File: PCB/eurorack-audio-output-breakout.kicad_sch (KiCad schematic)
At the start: 23 parts, among them J1 upper, J2 lower, J3 Conn_01x04_Pin, J4 Conn_01x02_Pin, J6 Conn_01x02_Pin, J7 Conn_01x02_Pin, J8 Conn_01x02_Pin, J9 Conn_01x02_Pin, U1 TL072

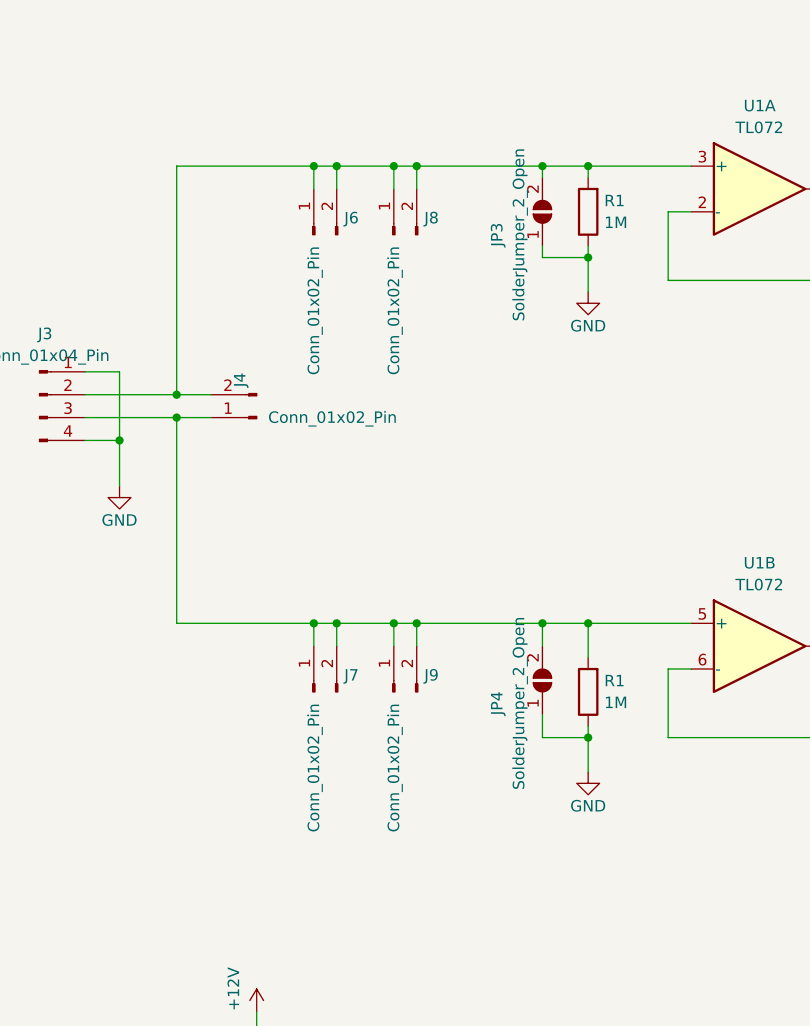
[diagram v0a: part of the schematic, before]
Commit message: Make the design slimmer
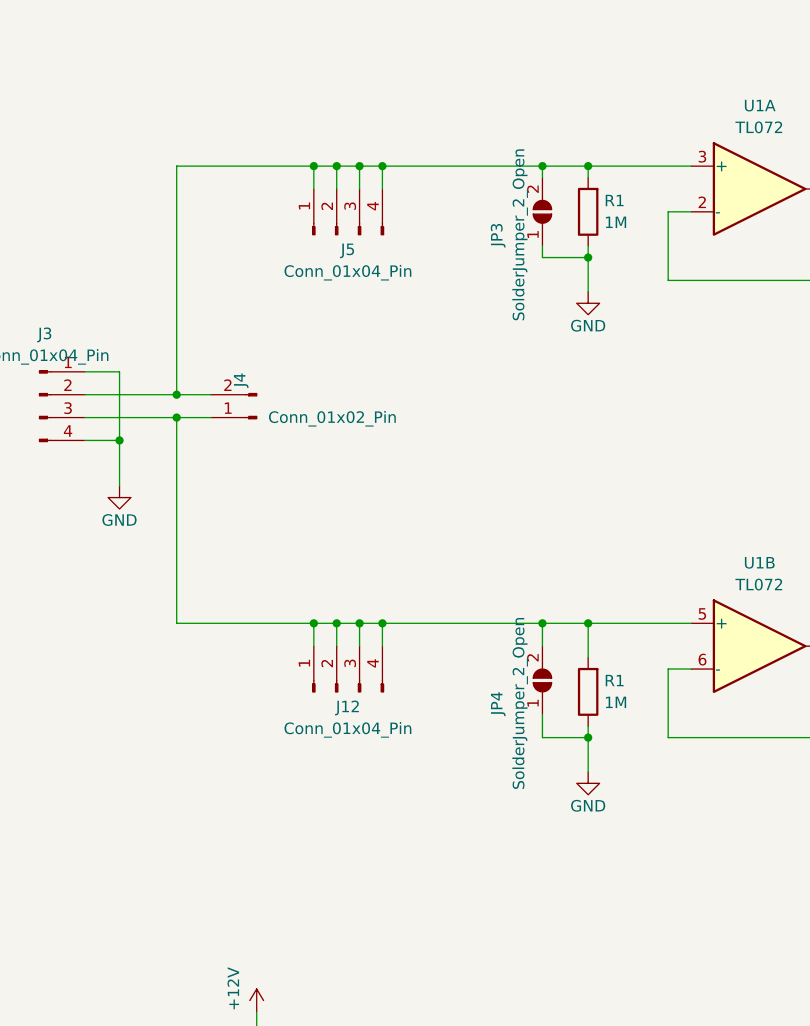
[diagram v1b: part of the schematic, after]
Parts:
- removed J6, J7, J8, J9: Conn_01x02_Pin, Connector_PinHeader_2.54mm:PinHeader_1x02_P2.54mm_Vertical, symbol Connector:Conn_01x02_Pin
- added J12, J5: Conn_01x04_Pin, Connector_PinHeader_2.54mm:PinHeader_1x04_P2.54mm_Vertical, symbol Connector:Conn_01x04_Pin
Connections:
- net at J3.3 (Pin_3), J4.1 (Pin_1), JP4.2 (B)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: now also J12.1 (Pin_1), J12.2 (Pin_2), J12.3 (Pin_3), J12.4 (Pin_4)
- net at J3.2 (Pin_2), J4.2 (Pin_2), JP3.2 (B)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: now also J5.1 (Pin_1), J5.2 (Pin_2), J5.3 (Pin_3), J5.4 (Pin_4)

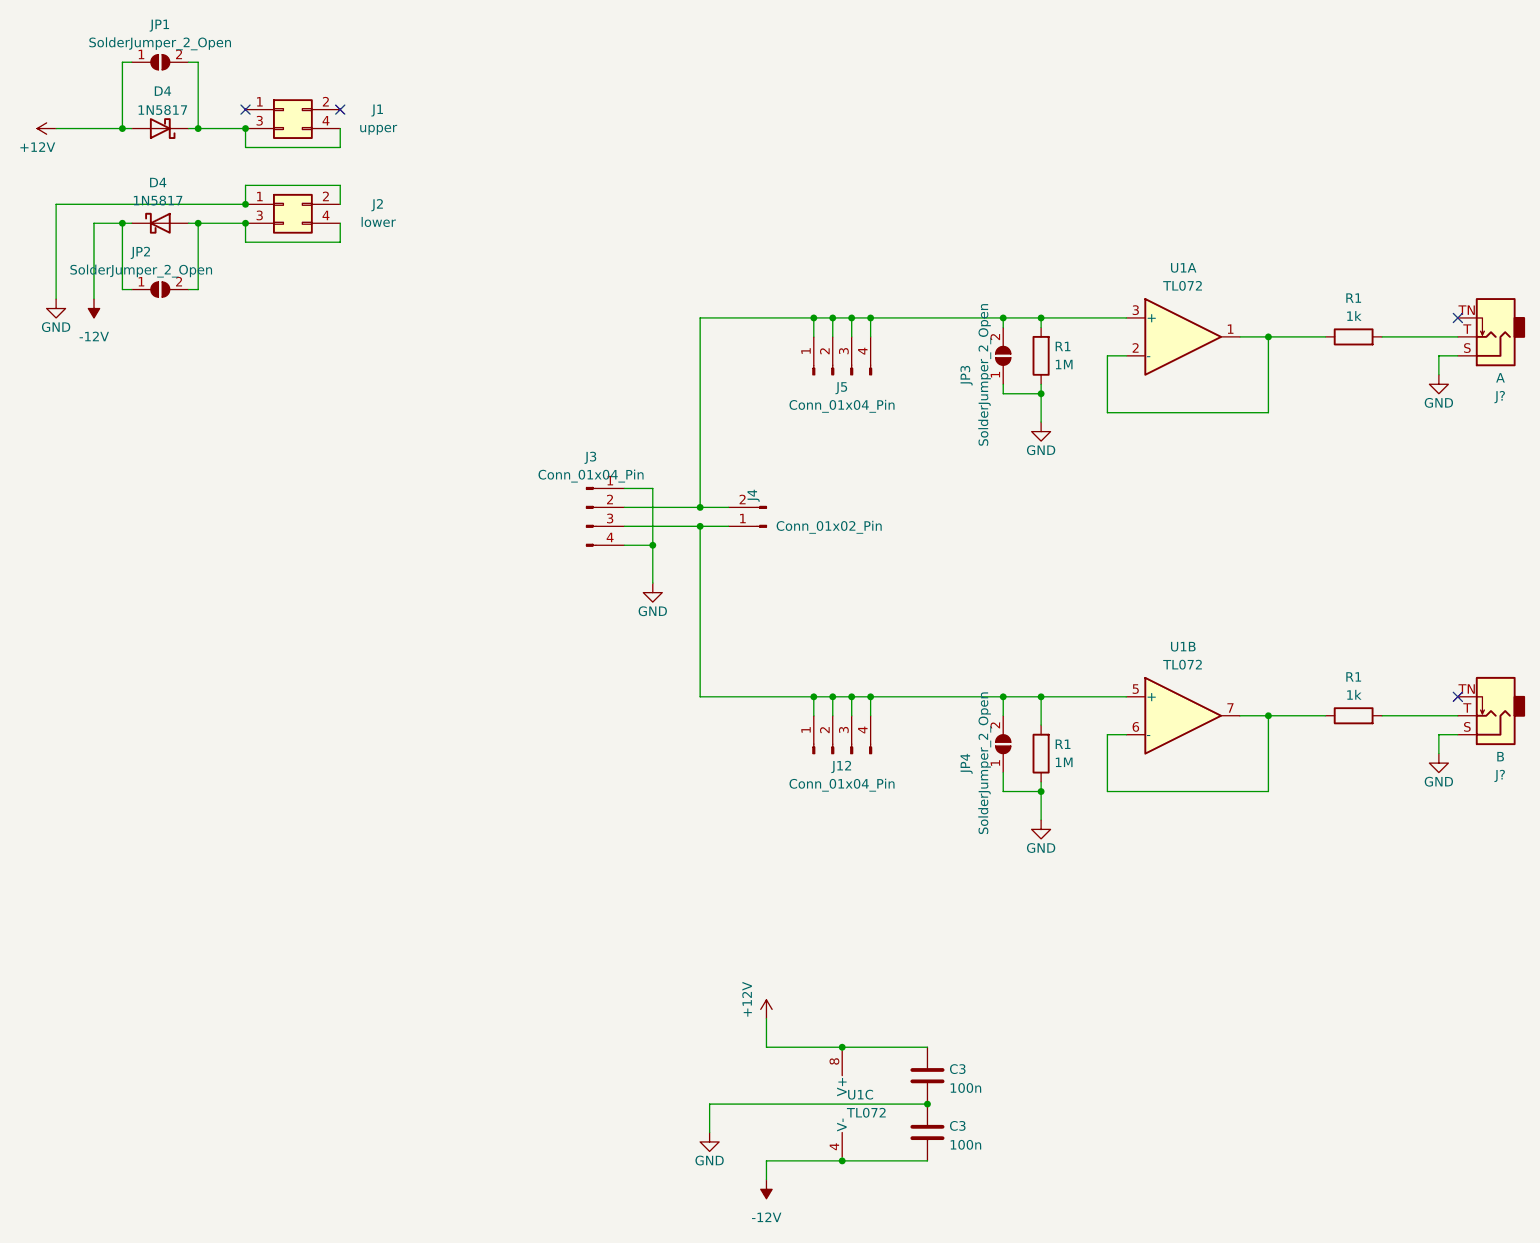
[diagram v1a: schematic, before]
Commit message: Remove some components and make PCB slimmer
Reverse protection and pull-down are not really needed in a
breadboard environment, as component placement needs care and
focus anyways. Remove these components and make the PCB slimmer.
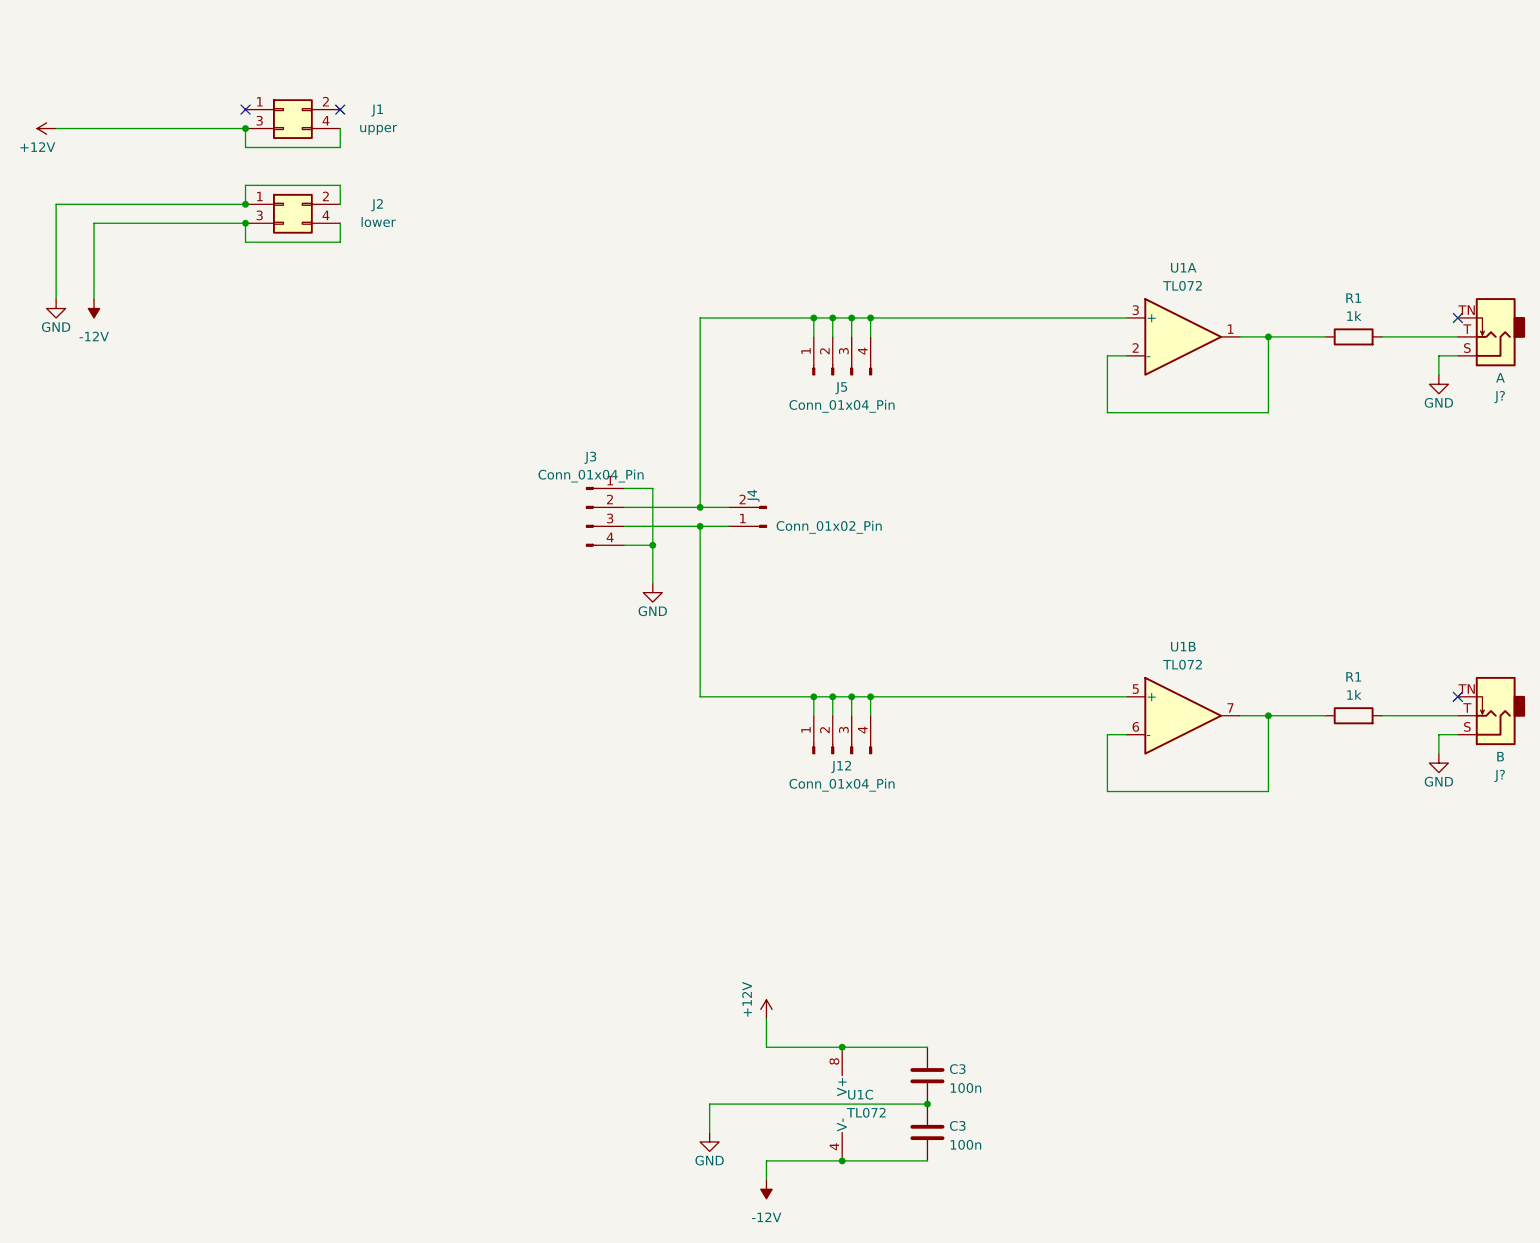
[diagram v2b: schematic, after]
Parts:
- removed D4 (x2): 1N5817, Diode_THT:D_DO-41_SOD81_P7.62mm_Horizontal, symbol Device:D_Schottky
- removed JP1, JP2, JP3, JP4: SolderJumper_2_Open, Jumper:SolderJumper-2_P1.3mm_Open_RoundedPad1.0x1.5mm, symbol Jumper:SolderJumper_2_Open
- removed R1 (x2): 1M, Resistor_THT:R_Axial_DIN0207_L6.3mm_D2.5mm_P7.62mm_Horizontal, symbol Device:R
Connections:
- net +12V: now also J1.3 (Pin_3), J1.4 (Pin_4)
- net -12V: now also J2.3 (Pin_3), J2.4 (Pin_4)

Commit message: Use part for breadboard power and fix spacing
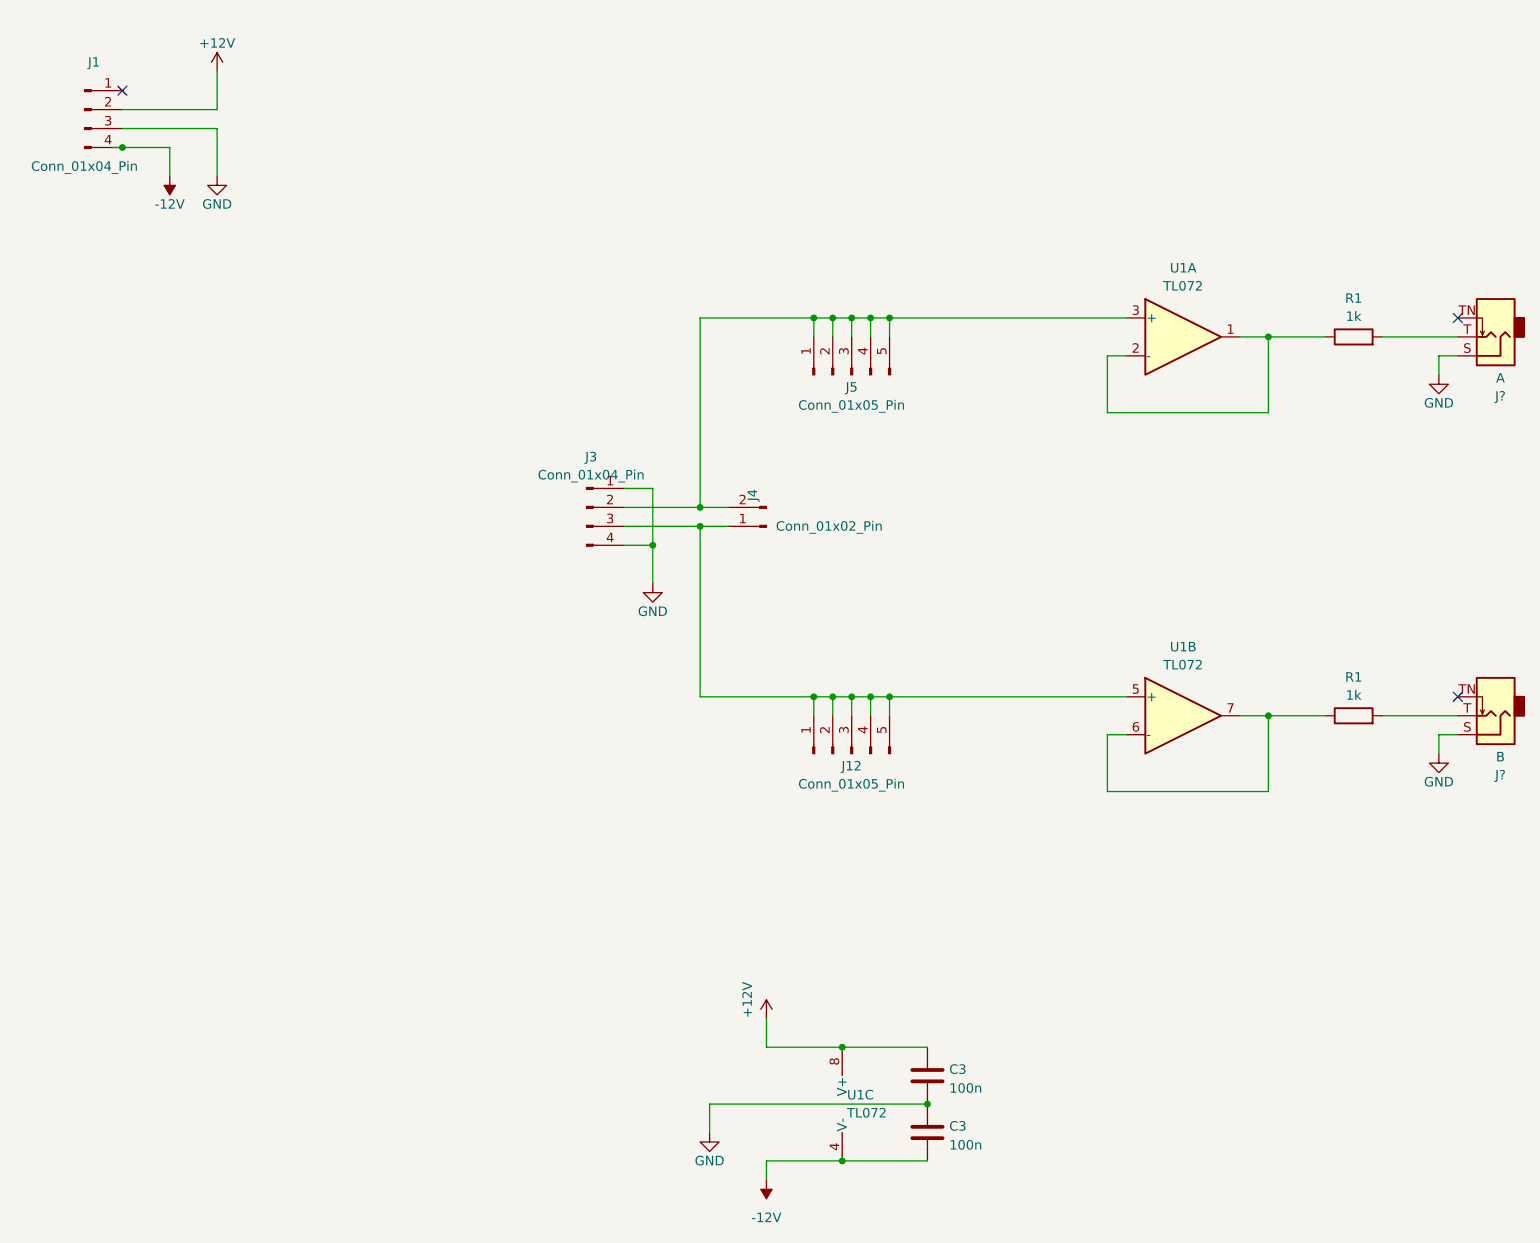
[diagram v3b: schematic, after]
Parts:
- removed J1: upper, Connector_PinHeader_2.54mm:PinHeader_2x02_P2.54mm_Vertical, symbol Connector_Generic:Conn_02x02_Odd_Even
- removed J12, J5: Conn_01x04_Pin, Connector_PinHeader_2.54mm:PinHeader_1x04_P2.54mm_Vertical, symbol Connector:Conn_01x04_Pin
- removed J2: lower, Connector_PinHeader_2.54mm:PinHeader_2x02_P2.54mm_Vertical, symbol Connector_Generic:Conn_02x02_Odd_Even
- added J1: Conn_01x04_Pin, moPsy:Breadboard Power Connector, symbol Connector:Conn_01x04_Pin
- added J12, J5: Conn_01x05_Pin, Connector_PinHeader_2.54mm:PinHeader_1x05_P2.54mm_Vertical, symbol Connector:Conn_01x05_Pin
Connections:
- net +12V: now also J1.2 (Pin_2)
- net -12V: now also J1.4 (Pin_4)
- net GND: now also J1.3 (Pin_3)
- net at J3.2 (Pin_2), J4.2 (Pin_2), U1.3 (+): now also J5.1 (Pin_1), J5.2 (Pin_2), J5.3 (Pin_3), J5.4 (Pin_4), J5.5 (Pin_5)
- net at J3.3 (Pin_3), J4.1 (Pin_1), U1.5 (+): now also J12.1 (Pin_1), J12.2 (Pin_2), J12.3 (Pin_3), J12.4 (Pin_4), J12.5 (Pin_5)
- no-connect marks 4 -> 3

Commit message: Fix U1 footprint
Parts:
- U1: footprint Package_DIP:DIP-8_W10.16mm -> Package_DIP:DIP-8_W7.62mm_Socket
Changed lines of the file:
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@@
       (effects (font (size 1.27 1.27)) (justify left))
     )
-    (property "Footprint" "Package_DIP:DIP-8_W10.16mm" (at 135.89 168.91 0)
+    (property "Footprint" "Package_DIP:DIP-8_W7.62mm_Socket" (at 135.89 168.91 0)
       (effects (font (size 1.27 1.27)) hide)
     )
@@
       (effects (font (size 1.27 1.27)))
     )
-    (property "Footprint" "Package_DIP:DIP-8_W10.16mm" (at 179.07 66.04 0)
+    (property "Footprint" "Package_DIP:DIP-8_W7.62mm_Socket" (at 179.07 66.04 0)
       (effects (font (size 1.27 1.27)) hide)
     )
@@
       (effects (font (size 1.27 1.27)))
     )
-    (property "Footprint" "Package_DIP:DIP-8_W10.16mm" (at 179.07 116.84 0)
-      (effects (font (size 1.27 1.27)) hide)
-    )
+    (property "Footprint" "Package_DIP:DIP-8_W7.62mm_Socket" (at 179.07 116.84 0)
+      (effects (font (size 1.27 1.27)) hide)
+    )
